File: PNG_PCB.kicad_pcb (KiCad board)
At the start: 2 copper layers, 109 parts, among them J1 screw term, J10 screw term, J11 screw term, J12 screw term, J13 screw term, J14 screw term, J15 screw term, J16 screw term, J17 screw term, J18 screw term, J19 screw term, J2 screw term, J20 screw term, J21 screw term, J22 screw term, J23 screw term, J24 screw term, J25 screw term, J26 screw term, J27 screw term, J28 screw term, J29 screw term, J3 screw term, J30 screw term, J4 screw term, J5 screw term, J6 screw term, J7 screw term, J8 screw term, J9 screw term, U1 Teensy4.1, U2 Mux, U3 MCP6004, U4 Mux, U5 Mux, U6 MCP6004, U7 Mux, U8 Mux, U9 MCP6004

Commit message: routed 3rd amp
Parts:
- moved J1 246.5 mm to (271.0, 261.4)
- moved J4 246.5 mm to (207.8, 231.6)
- moved J5 246.5 mm to (206.2, 269.5)
- moved J6 246.5 mm to (207.0, 250.2)
- moved J2 246.5 mm to (248.4, 271.3)
- moved J3 246.5 mm to (248.2, 255.8)
- moved U2 246.5 mm to (226.6, 252.7)
- moved R16 180.2 mm to (148.8, 166.4)
- moved R15 170.8 mm to (153.9, 170.2), turned to 180 degrees
- moved R21 169.9 mm to (159.0, 166.4)
- moved R19 169.7 mm to (153.9, 174.0), turned to 180 degrees
- moved R18 165.1 mm to (159.0, 170.2)
- moved R20 163.8 mm to (159.0, 174.0)
- moved J11 103.5 mm to (305.1, 204.7)
- moved J9 103.5 mm to (307.3, 181.9)
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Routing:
- net +3V3: track 0.00 -> 36.7 mm
- net /ampB0/V1: track 0.00 -> 30.8 mm
- net Net-(R5-Pad1): track 0.00 -> 17.6 mm
- net Net-(R12-Pad1): track 0.00 -> 17.6 mm
- net Net-(R19-Pad1): track 0.00 -> 17.6 mm
- net Net-(R26-Pad1): track 0.00 -> 17.3 mm
- net /ampD0/V1: track 0.00 -> 16.3 mm
- net /ampA0/V1: track 0.00 -> 15.5 mm
- net Net-(R4-Pad2): track 0.00 -> 7.62 mm
- net Net-(R25-Pad2): track 0.00 -> 7.62 mm
- net Net-(R18-Pad2): track 0.00 -> 7.62 mm
- net Net-(R11-Pad2): track 0.00 -> 7.62 mm
- net /ampD0/V2: track 0.00 -> 7.62 mm
- net /ampC0/V2: track 0.00 -> 7.62 mm
- net /ampB0/V2: track 0.00 -> 7.62 mm
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
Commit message: placed final location of call components
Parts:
- moved J1 157.7 mm to (159.5, 149.9), turned to 270 degrees
- moved J2 146.8 mm to (165.9, 149.9), turned to 270 degrees
- moved J3 130.3 mm to (172.2, 149.9), turned to 270 degrees
- moved J5 122.8 mm to (178.6, 149.9), turned to 270 degrees
- moved U2 120.2 mm to (198.4, 135.9), turned to 180 degrees
- moved J7 119.1 mm to (197.6, 149.9), turned to 270 degrees
- moved J6 102.7 mm to (184.9, 149.9), turned to 270 degrees
- moved J9 102.2 mm to (210.3, 149.9), turned to 270 degrees
- moved J11 93.5 mm to (229.4, 149.9), turned to 270 degrees
- moved U4 87.1 mm to (215.9, 135.9), turned to 180 degrees
- moved J4 83.4 mm to (191.3, 149.9), turned to 270 degrees
- moved J10 70.8 mm to (216.7, 149.9), turned to 270 degrees
- moved J8 70.1 mm to (204.0, 149.9), turned to 270 degrees
- moved J12 52.8 mm to (223.0, 149.9), turned to 270 degrees
- moved R24 35.1 mm to (178.8, 136.9)
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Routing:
- net /ampA0/mux0: track 0.00 -> 41.2 mm
- net +3V3: track 36.7 -> 0.00 mm
- net /ampA0/mux1: track 0.00 -> 32.8 mm
- net /ampB0/mux1: track 0.00 -> 32.3 mm
- net /ampC0/V1: track 0.00 -> 31.2 mm
- net /ampD0/mux1: track 0.00 -> 29.7 mm
- net /ampC0/mux0: track 0.00 -> 28.5 mm
- net /ampB2/V1: track 57.4 -> 30.9 mm
- net /ampA2/V1: track 40.1 -> 14.3 mm
- net /ampA0/mux2: track 0.00 -> 25.4 mm
- net /ampB0/mux2: track 0.00 -> 22.1 mm
- net /ampC0/mux1: track 0.00 -> 20.8 mm
- net /ampD0/mux2: track 0.00 -> 19.5 mm
- net /ampC0/mux2: track 0.00 -> 17.4 mm
- net /ampB0/mux0: track 0.00 -> 16.9 mm
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
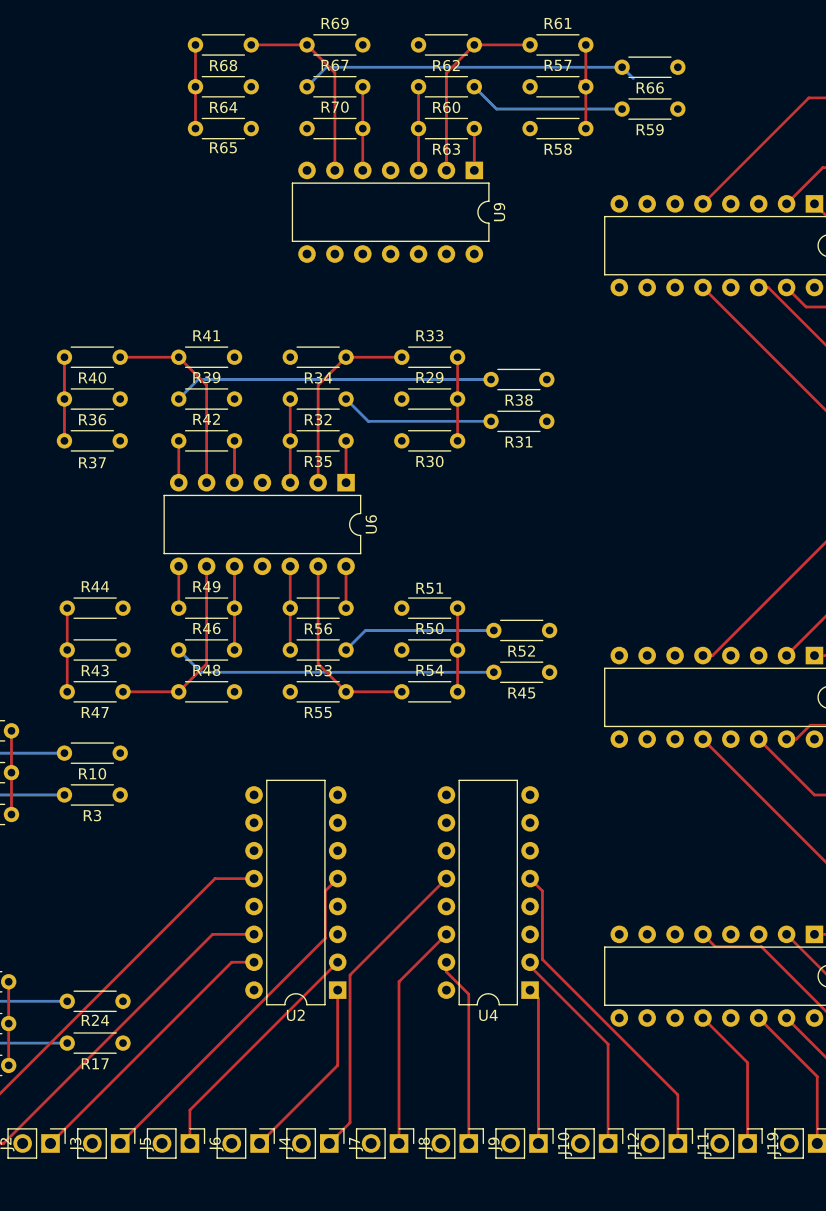
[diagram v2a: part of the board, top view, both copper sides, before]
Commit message: routed sel lines to muxes
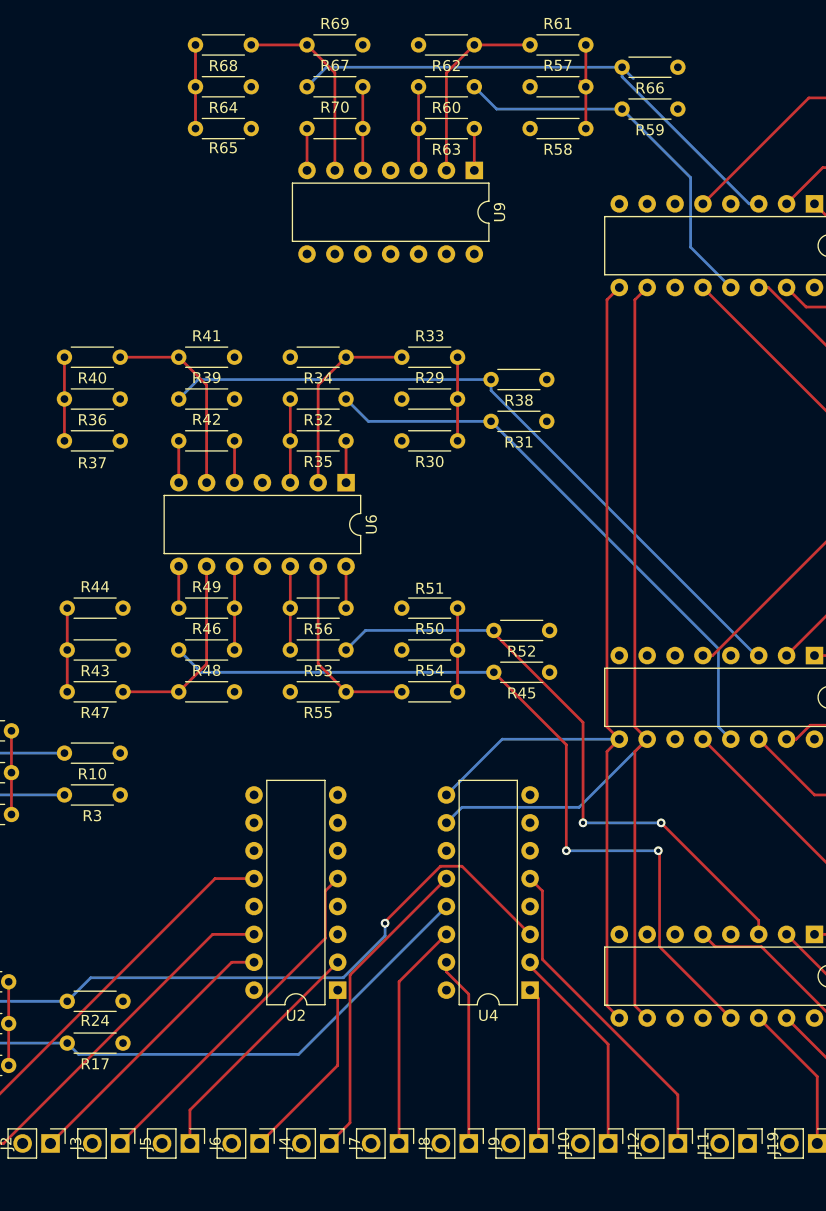
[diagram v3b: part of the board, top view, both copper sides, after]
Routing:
- net /selA: track 0.00 -> 89.9 mm
- net /selB: track 0.00 -> 86.3 mm
- net /ampD0/V1: track 16.1 -> 66.7 mm, vias 0 -> 1
- net /ampC1/V1: track 29.5 -> 74.9 mm, vias 0 -> 2
- net /ampD1/V1: track 14.2 -> 56.0 mm, vias 0 -> 2
- net /ampC0/V1: track 31.2 -> 71.8 mm
- net /ampA1/V1: track 14.0 -> 52.1 mm
- net /ampB1/V1: track 29.2 -> 64.6 mm
- net /ampA2/V1: track 14.3 -> 34.7 mm
- net /ampB2/V1: track 30.9 -> 49.0 mm
- net /ampC1/mux0: track 13.1 -> 0.00 mm
- net /ADC_IN_9: track 0.00 -> 3.81 mm
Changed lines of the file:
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@@
     (thickness 1.6)
     (drawings 0)
-    (tracks 167)
+    (tracks 223)
     (zones 0)
     (modules 109)
@@
   (segment (start 145.034 140.716) (end 143.256 138.938) (width 0.25) (layer B.Cu) (net 19))
   (segment (start 173.736 140.716) (end 145.034 140.716) (width 0.25) (layer B.Cu) (net 19))
+  (segment (start 194.808999 141.741001) (end 208.28 128.27) (width 0.25) (layer B.Cu) (net 19))
+  (segment (start 174.761001 141.741001) (end 194.808999 141.741001) (width 0.25) (layer B.Cu) (net 19))
+  (segment (start 173.736 140.716) (end 174.761001 141.741001) (width 0.25) (layer B.Cu) (net 19))
   (segment (start 143.256 135.128) (end 143.256 131.318) (width 0.25) (layer F.Cu) (net 20))
   (segment (start 216.662 136.652) (end 215.9 135.89) (width 0.25) (layer F.Cu) (net 21))
@@
   (segment (start 160.528 136.906) (end 158.496 138.938) (width 0.25) (layer B.Cu) (net 25))
   (segment (start 173.736 136.906) (end 160.528 136.906) (width 0.25) (layer B.Cu) (net 25))
+  (via (at 202.692 129.794) (size 0.8) (drill 0.4) (layers F.Cu B.Cu) (net 25))
+  (segment (start 202.692 129.652998) (end 202.692 129.794) (width 0.25) (layer F.Cu) (net 25))
+  (segment (start 207.739999 124.604999) (end 202.692 129.652998) (width 0.25) (layer F.Cu) (net 25))
+  (segment (start 209.694999 124.604999) (end 207.739999 124.604999) (width 0.25) (layer F.Cu) (net 25))
+  (segment (start 215.9 130.81) (end 209.694999 124.604999) (width 0.25) (layer F.Cu) (net 25))
+  (segment (start 198.882 134.764999) (end 175.877001 134.764999) (width 0.25) (layer B.Cu) (net 25))
+  (segment (start 202.692 130.954999) (end 198.882 134.764999) (width 0.25) (layer B.Cu) (net 25))
+  (segment (start 175.877001 134.764999) (end 173.736 136.906) (width 0.25) (layer B.Cu) (net 25))
+  (segment (start 202.692 129.794) (end 202.692 130.954999) (width 0.25) (layer B.Cu) (net 25))
   (segment (start 158.496 131.318) (end 158.496 135.128) (width 0.25) (layer F.Cu) (net 26))
   (segment (start 243.078 124.46) (end 231.648 113.03) (width 0.25) (layer F.Cu) (net 27))
@@
   (segment (start 201.168 84.074) (end 199.136 82.042) (width 0.25) (layer B.Cu) (net 31))
   (segment (start 212.344 84.074) (end 201.168 84.074) (width 0.25) (layer B.Cu) (net 31))
+  (segment (start 233.062999 111.904999) (end 234.188 113.03) (width 0.25) (layer B.Cu) (net 31))
+  (segment (start 233.062999 104.792999) (end 233.062999 111.904999) (width 0.25) (layer B.Cu) (net 31))
+  (segment (start 212.344 84.074) (end 233.062999 104.792999) (width 0.25) (layer B.Cu) (net 31))
   (segment (start 199.136 85.852) (end 199.136 89.662) (width 0.25) (layer F.Cu) (net 32))
   (segment (start 252.222 105.41) (end 241.808 105.41) (width 0.25) (layer F.Cu) (net 33))
@@
   (segment (start 185.674 80.264) (end 183.896 82.042) (width 0.25) (layer B.Cu) (net 37))
   (segment (start 212.344 80.264) (end 185.674 80.264) (width 0.25) (layer B.Cu) (net 37))
+  (segment (start 236.500051 105.41) (end 236.728 105.41) (width 0.25) (layer B.Cu) (net 37))
+  (segment (start 212.344 81.253949) (end 236.500051 105.41) (width 0.25) (layer B.Cu) (net 37))
+  (segment (start 212.344 80.264) (end 212.344 81.253949) (width 0.25) (layer B.Cu) (net 37))
   (segment (start 183.896 85.852) (end 183.896 89.662) (width 0.25) (layer F.Cu) (net 38))
-  (segment (start 235.712 142.494) (end 231.648 138.43) (width 0.25) (layer F.Cu) (net 39))
-  (segment (start 235.712 149.86) (end 235.712 142.494) (width 0.25) (layer F.Cu) (net 39))
   (segment (start 242.062 143.764) (end 236.728 138.43) (width 0.25) (layer F.Cu) (net 40))
   (segment (start 242.062 149.86) (end 242.062 143.764) (width 0.25) (layer F.Cu) (net 40))
@@
   (segment (start 185.928 106.934) (end 183.896 104.902) (width 0.25) (layer B.Cu) (net 43))
   (segment (start 212.598 106.934) (end 185.928 106.934) (width 0.25) (layer B.Cu) (net 43))
+  (segment (start 227.693001 123.299001) (end 227.584 123.19) (width 0.25) (layer F.Cu) (net 43))
+  (segment (start 227.693001 131.935001) (end 227.693001 123.299001) (width 0.25) (layer F.Cu) (net 43))
+  (via (at 227.584 123.19) (size 0.8) (drill 0.4) (layers F.Cu B.Cu) (net 43))
+  (segment (start 234.188 138.43) (end 227.693001 131.935001) (width 0.25) (layer F.Cu) (net 43))
+  (via (at 219.202 123.19) (size 0.8) (drill 0.4) (layers F.Cu B.Cu) (net 43))
+  (segment (start 227.584 123.19) (end 219.202 123.19) (width 0.25) (layer B.Cu) (net 43))
+  (segment (start 219.202 113.538) (end 212.598 106.934) (width 0.25) (layer F.Cu) (net 43))
+  (segment (start 219.202 123.19) (end 219.202 113.538) (width 0.25) (layer F.Cu) (net 43))
   (segment (start 183.896 97.282) (end 183.896 101.092) (width 0.25) (layer F.Cu) (net 44))
   (segment (start 241.808 130.81) (end 252.222 130.81) (width 0.25) (layer F.Cu) (net 45))
@@
   (segment (start 200.914 103.124) (end 199.136 104.902) (width 0.25) (layer B.Cu) (net 49))
   (segment (start 212.598 103.124) (end 200.914 103.124) (width 0.25) (layer B.Cu) (net 49))
+  (via (at 227.838 120.65) (size 0.8) (drill 0.4) (layers F.Cu B.Cu) (net 49))
+  (segment (start 236.728 129.54) (end 227.838 120.65) (width 0.25) (layer F.Cu) (net 49))
+  (segment (start 236.728 130.81) (end 236.728 129.54) (width 0.25) (layer F.Cu) (net 49))
+  (via (at 220.726 120.65) (size 0.8) (drill 0.4) (layers F.Cu B.Cu) (net 49))
+  (segment (start 227.838 120.65) (end 220.726 120.65) (width 0.25) (layer B.Cu) (net 49))
+  (segment (start 212.598 103.371002) (end 212.598 103.124) (width 0.25) (layer F.Cu) (net 49))
+  (segment (start 220.726 111.499002) (end 212.598 103.371002) (width 0.25) (layer F.Cu) (net 49))
+  (segment (start 220.726 120.65) (end 220.726 111.499002) (width 0.25) (layer F.Cu) (net 49))
   (segment (start 199.136 97.282) (end 199.136 101.092) (width 0.25) (layer F.Cu) (net 50))
   (segment (start 246.126 86.36) (end 231.648 71.882) (width 0.25) (layer F.Cu) (net 51))
@@
   (segment (start 212.852 55.626) (end 210.82 53.594) (width 0.25) (layer B.Cu) (net 55))
   (segment (start 224.282 55.626) (end 212.852 55.626) (width 0.25) (layer B.Cu) (net 55))
+  (segment (start 230.522999 68.216999) (end 234.188 71.882) (width 0.25) (layer B.Cu) (net 55))
+  (segment (start 230.522999 61.866999) (end 230.522999 68.216999) (width 0.25) (layer B.Cu) (net 55))
+  (segment (start 224.282 55.626) (end 230.522999 61.866999) (width 0.25) (layer B.Cu) (net 55))
   (segment (start 210.82 57.404) (end 210.82 61.214) (width 0.25) (layer F.Cu) (net 56))
   (segment (start 244.856 67.31) (end 241.808 64.262) (width 0.25) (layer F.Cu) (net 57))
@@
   (segment (start 224.282 51.816) (end 197.358 51.816) (width 0.25) (layer B.Cu) (net 61))
   (segment (start 224.282 51.816) (end 225.307001 52.841001) (width 0.25) (layer B.Cu) (net 61))
+  (segment (start 235.853002 64.262) (end 236.728 64.262) (width 0.25) (layer B.Cu) (net 61))
+  (segment (start 224.282 52.690998) (end 235.853002 64.262) (width 0.25) (layer B.Cu) (net 61))
+  (segment (start 224.282 51.816) (end 224.282 52.690998) (width 0.25) (layer B.Cu) (net 61))
+  (segment (start 195.58 57.404) (end 195.58 61.214) (width 0.25) (layer F.Cu) (net 62))
+  (segment (start 225.442999 111.904999) (end 226.568 113.03) (width 0.25) (layer F.Cu) (net 63))
+  (segment (start 225.442999 73.007001) (end 225.442999 111.904999) (width 0.25) (layer F.Cu) (net 63))
+  (segment (start 226.568 71.882) (end 225.442999 73.007001) (width 0.25) (layer F.Cu) (net 63))
+  (segment (start 225.442999 137.304999) (end 226.568 138.43) (width 0.25) (layer F.Cu) (net 63))
+  (segment (start 226.568 113.03) (end 225.442999 114.155001) (width 0.25) (layer F.Cu) (net 63))
+  (segment (start 225.442999 114.155001) (end 225.442999 137.304999) (width 0.25) (layer F.Cu) (net 63))
+  (segment (start 209.694999 119.235001) (end 208.28 120.65) (width 0.25) (layer B.Cu) (net 63))
+  (segment (start 220.362999 119.235001) (end 209.694999 119.235001) (width 0.25) (layer B.Cu) (net 63))
+  (segment (start 226.568 113.03) (end 220.362999 119.235001) (width 0.25) (layer B.Cu) (net 63))
+  (segment (start 222.902999 137.304999) (end 224.028 138.43) (width 0.25) (layer F.Cu) (net 64))
+  (segment (start 222.902999 114.155001) (end 222.902999 137.304999) (width 0.25) (layer F.Cu) (net 64))
+  (segment (start 224.028 113.03) (end 222.902999 114.155001) (width 0.25) (layer F.Cu) (net 64))
+  (segment (start 213.36 113.03) (end 208.28 118.11) (width 0.25) (layer B.Cu) (net 64))
+  (segment (start 224.028 113.03) (end 213.36 113.03) (width 0.25) (layer B.Cu) (net 64))
+  (segment (start 222.902999 111.904999) (end 224.028 113.03) (width 0.25) (layer F.Cu) (net 64))
+  (segment (start 222.902999 73.007001) (end 222.902999 111.904999) (width 0.25) (layer F.Cu) (net 64))
+  (segment (start 224.028 71.882) (end 222.902999 73.007001) (width 0.25) (layer F.Cu) (net 64))
   (segment (start 188.976 85.852) (end 188.976 89.662) (width 0.25) (layer F.Cu) (net 71))
   (segment (start 178.562 78.232) (end 183.896 78.232) (width 0.25) (layer F.Cu) (net 72))

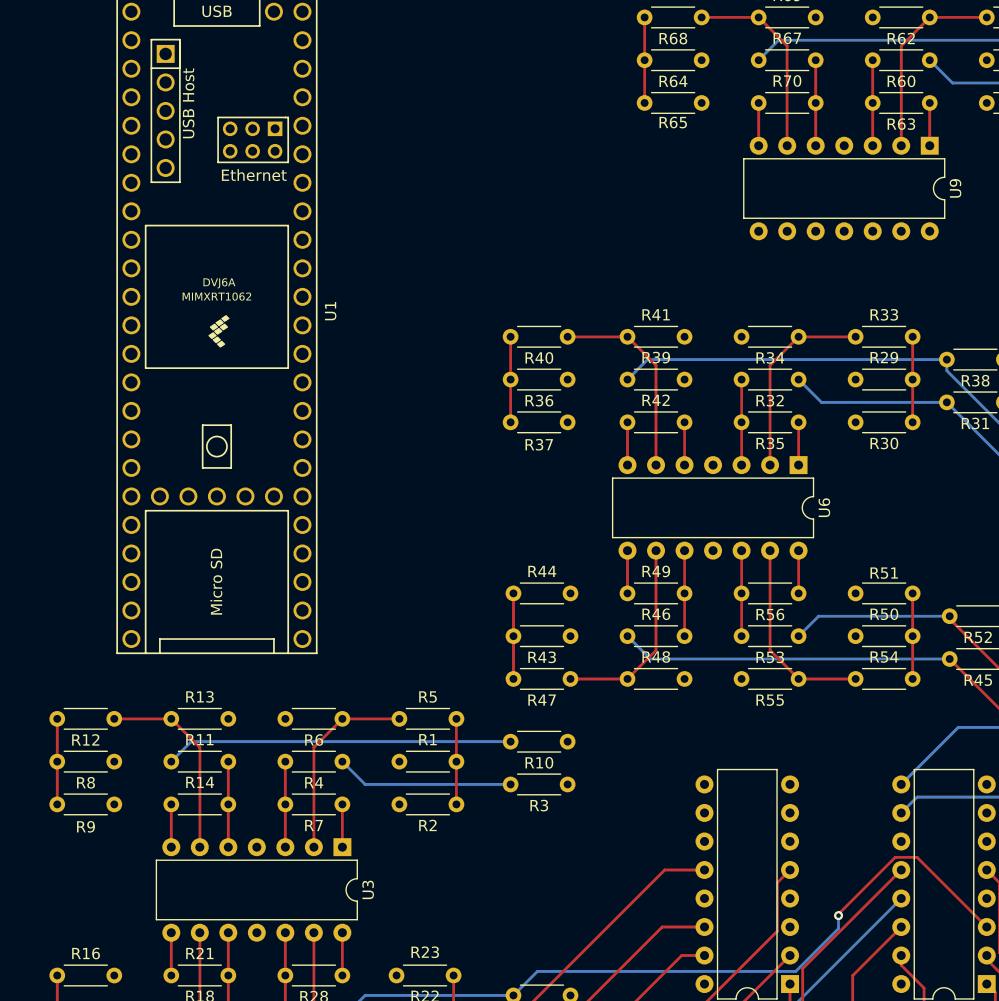
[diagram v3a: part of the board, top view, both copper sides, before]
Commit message: all components placed and routed
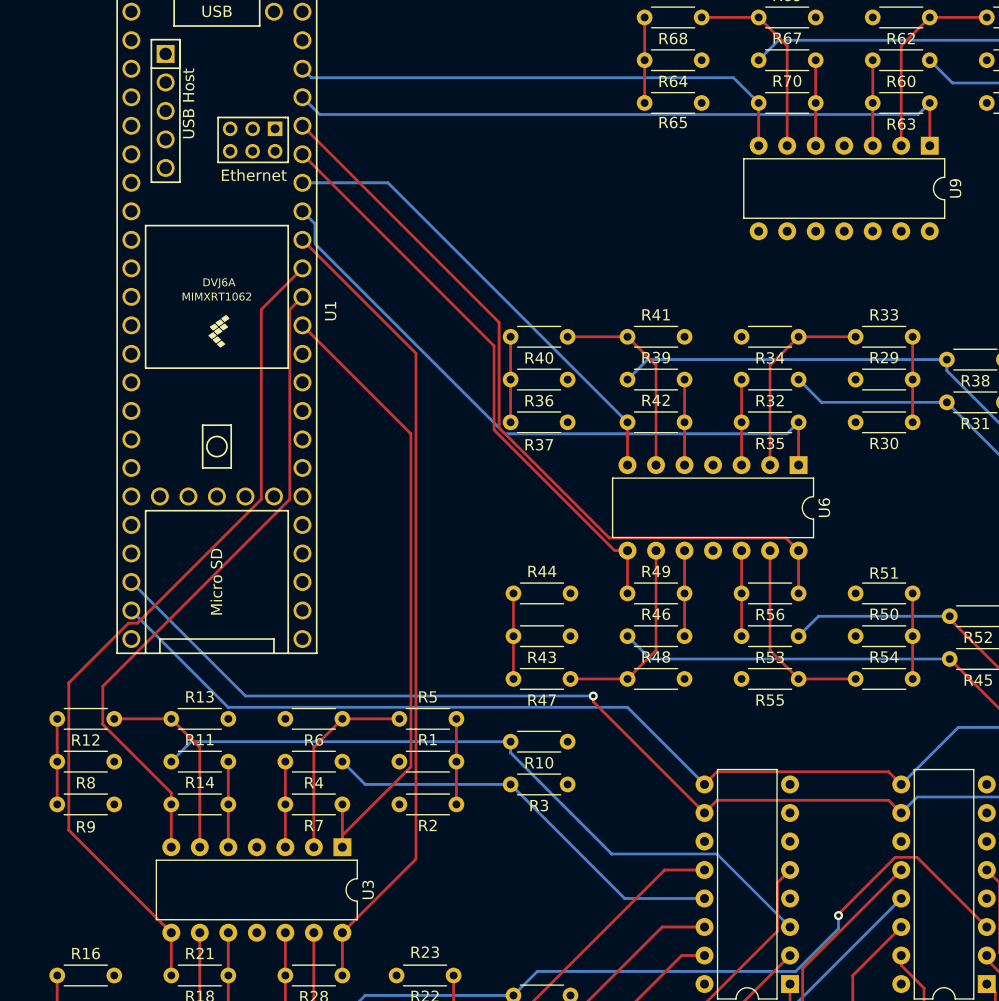
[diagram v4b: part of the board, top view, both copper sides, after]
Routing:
- net /selA: track 89.9 -> 168.2 mm, vias 0 -> 1
- net /selB: track 86.3 -> 162.2 mm
- net /ADC_IN_2: track 3.81 -> 75.9 mm
- net /ADC_IN_3: track 3.81 -> 72.4 mm
- net /ADC_IN_7: track 3.81 -> 69.2 mm
- net /ADC_IN_8: track 3.81 -> 60.7 mm
- net /ADC_IN_1: track 3.81 -> 58.9 mm
- net /ADC_IN_4: track 3.81 -> 57.7 mm
- net /ADC_IN_0: track 3.81 -> 56.8 mm
- net /ADC_IN_6: track 3.81 -> 51.8 mm
- net /ADC_IN_9: track 3.81 -> 45.7 mm
- net /ADC_IN_5: track 3.81 -> 41.6 mm
- net /ampB0/V1: track 31.0 -> 63.3 mm
- net /ampA0/V1: track 15.8 -> 37.3 mm
- net Net-(R39-Pad2): track 3.81 -> 7.62 mm
